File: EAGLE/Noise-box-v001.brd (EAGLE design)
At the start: 160 x 100 mm, 41 parts, among them J1 AVR_SPI_PROG_3X22X3_LOCK, J2 BATT, J4 MICRO-SD_CARD_SOCKET, J5 AUDIO_JACK_3.5MM_SMD, U1 ATMEGA328P_TQFP, U2 MIC5219 3.3V, U3 MCP73831, Y1 12.288MHz

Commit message: Battery
Picked battery with best available Wh/dollar
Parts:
- removed J2: BATT, SparkFun-Connectors:JST-2-SMD
- removed J3: (no value), SparkFun-Connectors:USB-MICROB
- added BT1: (no value), SparkFun-Batteries:BATTERY_18650-HOLDER
- added C16, C21, C23: 1.0uF, SparkFun-Capacitors:0603
- added C17, C18, C19, C20: 1nF, SparkFun-Capacitors:0603
- added C22: 0.1uF, SparkFun-Capacitors:0603
- added J6: POWER_JACK, SparkFun-Connectors:POWER_JACK_PTH
- added L1, L2, L3, L4: (no value), SparkFun-Coils:0805
- added Y2: 8MHz, SparkFun-Clocks:RESONATOR-SMD-3.2X1.3
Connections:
- removed net VIN: C5.1, J3.VBUS, R2.1, U3.4
- new net 0V: BT1.GND@1, C6.2, J6.GNDBREAK, R3.1, R4.1, U3.2
- new net N$10: L2.1, U$4.14
- new net N$11: L3.1, U$4.11
- new net N$12: L4.1, U$4.10
- new net N$23: U1.14
- new net N$25: U1.12
- new net N$26: U1.11
- new net N$27: U1.10
- new net N$28: U1.9
- new net N$29: U1.2
- new net N$30: U1.1
- new net N$31: U1.32
- new net N$32: U1.31
- new net N$33: U1.30
- new net N$36: U1.28
- new net N$37: U1.27
- new net N$38: U1.26
- new net N$39: U1.25
- new net N$40: U1.24
- new net N$41: U1.23
- new net N$5: U1.7, Y2.1
- new net N$8: U1.8, Y2.3
- new net N$9: L1.1, U$4.15
- new net SPKL+: C17.1, L4.2
- new net SPKL-: C18.1, L3.2
- new net SPKR+: C20.1, L1.2
- new net SPKR-: C19.1, L2.2
- net +3V3: now also C16.1, C21.1, C22.1, C23.1, U$4.16, U$4.9
- net GND: now also C16.2, C17.2, C18.2, C19.2, C20.2, C21.2, C22.2, C23.2, J6.GND, Y2.2; no longer C6.2, J2.2, J3.GND, R3.1, R4.1, U3.2
- net LEFT: now also U1.22
- net MISO: now also U1.16
- net MOSI: now also U1.15
- net RIGHT: now also U1.19
- net SCK: now also U1.17
- net SD-CS: now also U1.13
- net V+: now also C5.1, J6.PWR, R2.1, U3.4
- net VBATT: now also BT1.PWR@1; no longer J2.1

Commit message: Layout
First pass at layout. Established rough board dimensions. It seems that
establishing GND different than Battery (-) will necessitate a long
trace through the middle of the board. This might be avoided by going
with a wire lead version of the battery holder and avoiding that
unwanted trace by use of wires.
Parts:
- added C24, C25, C26, C27: 0.1uF, SparkFun-Capacitors:0603
- added J2, J3: (no value), SparkFun-Connectors:1X02_2.54_SCREWTERM
- added S2: UP, SparkFun-Switches:TACTILE_SWITCH_PTH_6.0MM
- added S3: DOWN, SparkFun-Switches:TACTILE_SWITCH_PTH_6.0MM
- R2: value 330k -> 470
- U$4: value (none) -> PAM84707
- moved C23 284.4 mm to (54.9, 24.4)
- moved C22 277.3 mm to (41.1, 27.2), turned to 90 degrees
- moved BT1 276.1 mm to (35.3, 25.9), flipped to the bottom
- moved C21 272.3 mm to (37.8, 36.7)
- moved Y2 269.4 mm to (41.1, 23.5), turned to 270 degrees
- moved C20 267.1 mm to (23.5, 40.1), turned to 180 degrees
- moved C19 264.6 mm to (29.3, 39.2), turned to 270 degrees
- moved C18 261.5 mm to (30.9, 39.2), turned to 270 degrees
- moved C17 260.7 mm to (36.7, 40.0)
- moved L4 255.5 mm to (34.0, 39.2), turned to 90 degrees
- moved J6 252.7 mm to (51.8, 1.78)
- moved L3 251.3 mm to (32.4, 39.2), turned to 90 degrees
- moved L2 246.1 mm to (27.8, 39.2), turned to 90 degrees
- moved L1 242.0 mm to (26.2, 39.2), turned to 90 degrees
- moved C16 234.8 mm to (22.6, 36.7), turned to 180 degrees
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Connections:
- new net AMP-L: C26.1
- new net AMP-R: C24.1
- new net AMP-SHDN: U$4.3
- new net N$13: J5.SLEEVE
- new net N$16: J5.RING
- new net N$19: J5.RSH
- new net N$20: J5.TSH
- new net N$22: J5.TIP
- new net N$24: C24.2, U$4.1
- new net N$34: C25.2, U$4.2
- new net N$35: C26.2, U$4.7
- new net N$42: C27.2, U$4.8
- new net N$43: S3.3, U$4.5
- new net N$44: S2.3, U$4.4
- net GBUF: now also C25.1, C27.1
- net GND: now also S2.1, S3.1
- net SPKL+: now also J2.P1
- net SPKL-: now also J2.P2
- net SPKR+: now also J3.P2
- net SPKR-: now also J3.P1
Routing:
- added copper zone on layer 1, net GND
- added copper zone on layer 16, net GND
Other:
- board size 160 x 100 mm -> 76.2 x 50.8 mm

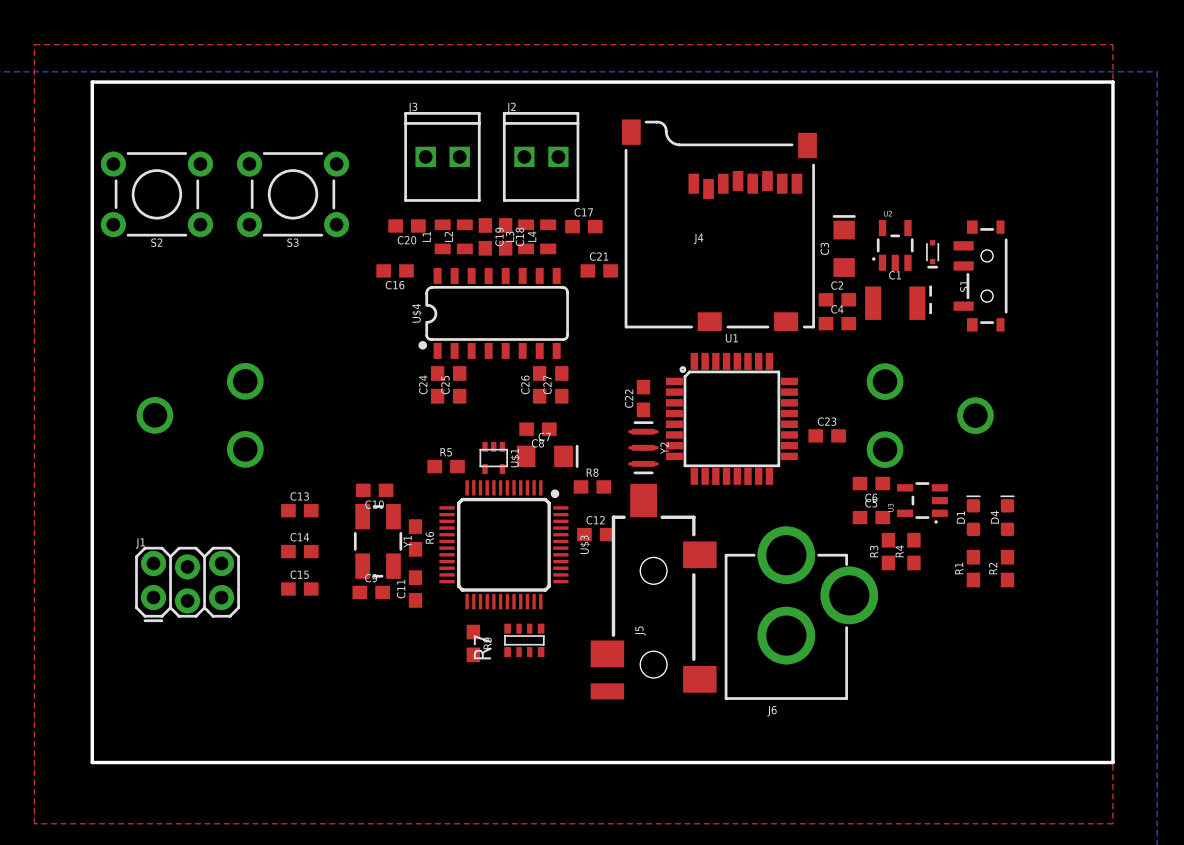
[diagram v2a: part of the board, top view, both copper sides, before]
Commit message: Layout updates
Adjusted battery holder package. Began layout, establishing rough
dimensions of the board.
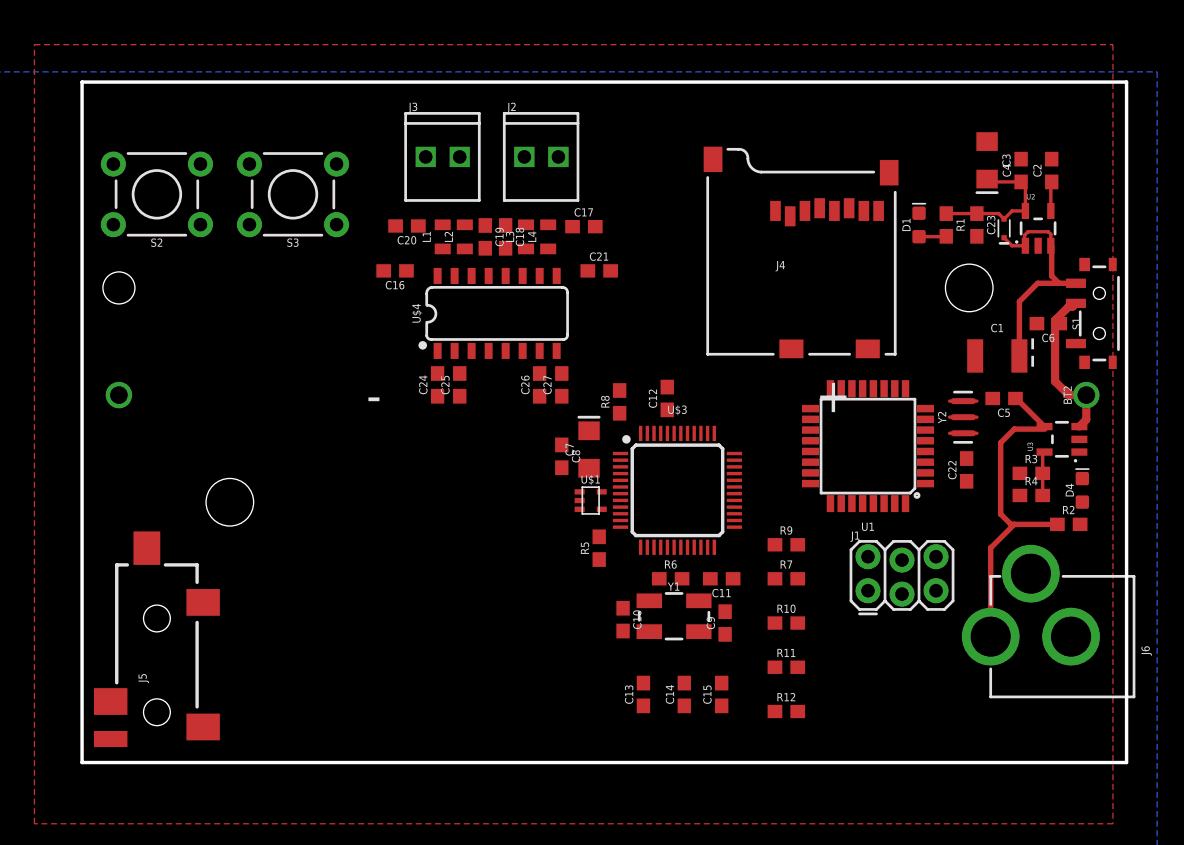
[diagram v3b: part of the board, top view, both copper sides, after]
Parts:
- removed BT1: (no value), SparkFun-Batteries:BATTERY_18650-HOLDER
- added BT2: (no value), MAK:BATTERY_18650-1043P
- added R10, R11, R12: 100k, SparkFun-Resistors:0603
- R7: value RN-4_100K -> 100k; device RJC-2:MNR14 -> SparkFun-Resistors:0603
- moved J1 53.3 mm to (57.9, 12.7)
- moved J5 37.3 mm to (4.83, 0.25)
- moved C15 32.5 mm to (47.0, 5.08), turned to 90 degrees
- moved C14 30.6 mm to (44.2, 5.08), turned to 90 degrees
- moved J6 29.9 mm to (80.8, 9.40), turned to 90 degrees
- moved C13 29.1 mm to (41.1, 5.08), turned to 90 degrees
- moved C9 26.5 mm to (47.2, 10.4), turned to 90 degrees
- moved R1 25.7 mm to (63.8, 40.1), turned to 270 degrees
- moved C22 24.7 mm to (65.3, 21.8)
- moved R9 24.5 mm to (51.8, 16.3), turned to 0 degrees
- moved Y2 24.0 mm to (65.0, 25.8), turned to 90 degrees
- moved C11 22.9 mm to (47.0, 13.7), turned to 180 degrees
- moved Y1 22.8 mm to (43.4, 10.9), turned to 0 degrees
- moved D1 22.2 mm to (61.7, 40.1)
- moved C10 20.9 mm to (39.6, 10.7), turned to 270 degrees
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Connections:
- removed net 0V: BT1.GND@1, C6.2, J6.GNDBREAK, R3.1, R4.1, U3.2
- removed net V+: C1.A, C5.1, D2.C, J6.PWR, R2.1, S1.1, U2.1, U2.3, U3.4
- new net N$45: C1.A, D2.C, S1.1, U2.1, U2.3
- new net VIN: C5.1, J6.PWR, R2.1, U3.4
- net EN-GPIO1: now also R11.2; no longer R7.6
- net GND: now also BT2.GND@1, C6.2, J6.GNDBREAK, R10.1, R11.1, R12.1, R3.1, R4.1, U3.2; no longer R7.2, R7.3, R7.4
- net GPIO0: now also R12.2; no longer R7.5
- net N$14: now also R7.2; no longer R7.8
- net N$15: now also R10.2; no longer R7.7
- net VBATT: now also BT2.PWR@1; no longer BT1.PWR@1
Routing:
- net VIN: track 0.00 -> 25.6 mm
- net N$45: track 0.00 -> 17.6 mm
- net VBATT: track 0.00 -> 12.0 mm
- net +3V3: track 0.00 -> 11.3 mm
- net N$4: track 0.00 -> 3.30 mm
- net N$2: track 0.00 -> 2.20 mm
- net N$3: track 0.00 -> 2.04 mm
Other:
- board size 76.2 x 50.8 mm -> 78 x 50.8 mm

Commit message: Layout
continued layout design. updated a few minor schematic errors
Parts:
- added C28, C29: 10nF, SparkFun-Capacitors:0603
- added C30: 47nF, SparkFun-Capacitors:0603
- added JP1: SJ1, SparkFun-Jumpers:SMT-JUMPER_2_NO_SILK
- added JP2: SJ2, SparkFun-Jumpers:SMT-JUMPER_2_NO_SILK
- added R13, R14, R15, R16, R17: 10, SparkFun-Resistors:0603
- added R18: 10k, SparkFun-Resistors:0603
- J5: value AUDIO_JACK_3.5MM_SMD -> HEADPHONE
- moved C11 51.7 mm to (2.54, 40.1), turned to 270 degrees
- moved R12 50.7 mm to (14.7, 38.4)
- moved C13 49.9 mm to (5.59, 40.1)
- moved C14 49.9 mm to (8.64, 40.1)
- moved R11 47.2 mm to (14.7, 36.3)
- moved R10 44.1 mm to (14.7, 34.3)
- moved C15 42.3 mm to (12.4, 29.5)
- moved J3 39.2 mm to (33.0, 6.86), turned to 180 degrees
- moved J2 38.8 mm to (26.4, 6.86), turned to 180 degrees
- moved S2 37.8 mm to (16.8, 6.60)
- moved C12 34.1 mm to (11.4, 40.1)
- moved C17 33.2 mm to (23.0, 9.78), flipped to the bottom, turned to 90 degrees
- moved C20 32.0 mm to (33.9, 9.78), flipped to the bottom, turned to 90 degrees
- moved C18 29.7 mm to (27.3, 9.78), flipped to the bottom, turned to 90 degrees
- moved R9 29.6 mm to (30.2, 36.6)
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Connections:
- removed net EN-GPIO1: R11.2, U$3.34
- removed net N$25: U1.12
- removed net N$26: U1.11
- removed net N$27: U1.10
- removed net N$31: U1.32
- removed net N$39: U1.25
- net +3V3: now also R18.2
- net AMP-L: now also J5.TSH, JP1.2
- net AMP-R: now also J5.RSH, JP2.2
- net AMP-SHDN: now also R11.2, U$3.34, U1.25
- net GBUF: now also J5.SLEEVE, R13.2
- net GND: now also C28.2, C29.2, C30.2
- net LEFT: now also J5.TIP, JP1.1, R16.2
- net MP3-CS: now also U1.10
- net MP3-DCS: now also U1.11
- net MP3-DREQ: now also U1.32
- net MP3-RST: now also U1.12
- net N$13: now also C28.1, R15.1; no longer J5.SLEEVE
- net N$16: now also C29.1, R14.1; no longer J5.RING
- net N$19: now also C30.1, R13.1; no longer J5.RSH
- net N$20: now also R15.2, R16.1; no longer J5.TSH
- net N$22: now also R14.2, R17.1; no longer J5.TIP
- net RIGHT: now also J5.RING, JP2.1, R17.2
- net RST: now also R18.1, U1.29
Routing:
- net SCK: track 0.00 -> 58.1 mm
- net +3V3: track 11.3 -> 58.0 mm
- net MISO: track 0.00 -> 46.1 mm
- net MOSI: track 0.00 -> 44.0 mm
- net RST: track 0.00 -> 33.0 mm
- net GBUF: track 0.00 -> 23.0 mm, vias 0 -> 1
- net N$44: track 0.00 -> 21.9 mm, vias 0 -> 1
- net N$24: track 0.00 -> 17.9 mm
- net VCC: track 0.00 -> 15.7 mm
- net N$43: track 0.00 -> 14.3 mm, vias 0 -> 1
- net LEFT: track 0.00 -> 12.5 mm, vias 0 -> 1
- net N$34: track 0.00 -> 11.9 mm
- net GND: track 0.00 -> 10.9 mm, vias 0 -> 3
- net N$35: track 0.00 -> 10.2 mm
- net N$18: track 0.00 -> 9.91 mm
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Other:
- board size 78 x 50.8 mm -> 80.5 x 40.1 mm
